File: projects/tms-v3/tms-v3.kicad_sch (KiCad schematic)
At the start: 55 parts, among them J1 ELEC_BATT, J10 XBee_R, J2 IGN_BATT, J3 LOAD_CELL, J4 PRESSURE, J5 ARM_SW, J6 IGNITER, J7 Teensy4.1_L, J8 Teensy4.1_R, J9 XBee_L, K1 HF46F, Q1 MMBT3904, U2A ADS1256_L, U2B ADS1256_R, U3 ADS1220IPWR, U4 LM7805, Y1 7.68MHz

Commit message: PCB workspace: scoped escape hatch, hardened gates, repo cleanup
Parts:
- removed D1: 1N4148WS, Diode_SMD:D_SOD-323, symbol Diode:1N4148WS
- removed J10: XBee_R, Connector_PinSocket_2.54mm:PinSocket_1x10_P2.54mm_Vertical, symbol Connector_Generic:Conn_01x10
- removed J9: XBee_L, Connector_PinSocket_2.54mm:PinSocket_1x10_P2.54mm_Vertical, symbol Connector_Generic:Conn_01x10
- removed K1: HF46F, symbol Connector_Generic:Conn_01x05
- removed Q1: MMBT3904, Package_TO_SOT_SMD:SOT-23, symbol Transistor_BJT:MMBT3904
- removed U2A: ADS1256_L, symbol Connector_Generic:Conn_01x14
- removed U2B: ADS1256_R, symbol Connector_Generic:Conn_01x14
- removed U3: ADS1220IPWR, Package_SO:TSSOP-16_4.4x5mm_P0.65mm, symbol Analog_ADC:ADS1220xPW
- removed U4: LM7805, Package_TO_SOT_SMD:TO-263-3_TabPin2, symbol Regulator_Linear:L7805
- removed Y1: 7.68MHz, Crystal:Crystal_HC49-U_Vertical, symbol Device:Crystal
- added C11: 100nF, Capacitor_SMD:C_0402_1005Metric, symbol Device:C
- added C14, C6: 100nF, Capacitor_SMD:C_0603_1608Metric, symbol Device:C
- added C17: 10uF, Capacitor_SMD:C_0805_2012Metric, symbol Device:C
- added D1: 1N4148WS, jlcpcb:SOD-323_L1.8-W1.3-LS2.5-RD-1, symbol jlcpcb:1N4148WS-C57759
- added D2: PESD5V0S2BT, jlcpcb:SOT-23_L2.9-W1.3-P1.90-LS2.4-BR, symbol jlcpcb:PESD5V0S2BT,215
- added D3: SS54, jlcpcb:SMA_L4.4-W2.8-LS5.4-R-RD, symbol jlcpcb:SS54_C22452
- added J9: XBEE3, tms:XBee_THT_20pin_P2.00mm, symbol Connector_Generic:Conn_02x10_Counter_Clockwise
- added K1: HF46F-G/5-HS1T, jlcpcb:RELAYS-TH_HF46F-G-XX-HS1-XXX, symbol jlcpcb:HF46F-G_5-HS1T_C5274026
- added L1: 10uH, Inductor_SMD:L_0805_2012Metric, symbol Device:L
- added Q1: MMBT3904, jlcpcb:SOT-23-3_L2.9-W1.3-P1.90-LS2.4-BR, symbol jlcpcb:MMBT3904-C20526
- added R10, R11, R12, R13, R14, R9: 33R, Resistor_SMD:R_0402_1005Metric, symbol Device:R
- added U2: ADS1256IDBR, jlcpcb:SSOP-28_L10.2-W5.3-P0.65-LS7.8-BL, symbol jlcpcb:ADS1256IDBR
- added U3: ADS1220IPWR, jlcpcb:TSSOP-16_L5.0-W4.4-P0.65-LS6.4-BL, symbol jlcpcb:ADS1220IPWR
- added U4: LM7805, jlcpcb:TO-263-2_L10.1-W9.1-P5.08-LS15.2-BR-1, symbol jlcpcb:LM7805_C22467097
- added Y1: 7.68MHz, jlcpcb:CRYSTAL-SMD_L11.4-W4.7-LS12.4, symbol jlcpcb:AT-41CD2-7.68MHZ
- C10: footprint Capacitor_SMD:C_0603_1608Metric -> Capacitor_SMD:C_0402_1005Metric
- C8, C9: value 22pF -> 33pF
- H1: value MH1 -> M3
- H2: value MH2 -> M3
- H3: value MH3 -> M3
- H4: value MH4 -> M3
- J1: value ELEC_BATT -> XT30PW-ELEC; footprint (none) -> Connector_AMASS:AMASS_XT30PW-F_1x02_P2.50mm_Horizontal
- J2: value IGN_BATT -> XT30PW-IGN; footprint (none) -> Connector_AMASS:AMASS_XT30PW-F_1x02_P2.50mm_Horizontal
- J3: value LOAD_CELL -> LOAD-CELL; footprint (none) -> Connector_JST:JST_XH_B5B-XH-A_1x05_P2.50mm_Vertical
- J4: footprint (none) -> Connector_JST:JST_XH_B3B-XH-A_1x03_P2.50mm_Vertical
- J5: value ARM_SW -> ARM-SW; footprint (none) -> TerminalBlock_Phoenix:TerminalBlock_Phoenix_MKDS-1,5-2-5.08_1x02_P5.08mm_Horizontal
- J6: value IGNITER -> IGN-OUT; footprint (none) -> Connector_AMASS:AMASS_XT60-F_1x02_P7.20mm_Vertical
- J7: value Teensy4.1_L -> TEENSY-L
- J8: value Teensy4.1_R -> TEENSY-R
- LED1: value PWR_GRN -> GREEN
- LED2: value ARM_RED -> RED
- LED3: value TX_YLW -> YELLOW
- TP1: value TP_VBAT -> VBAT
- TP2: value TP_5V -> +5V
- TP3: value TP_3V3 -> +3V3
- TP4: value TP_AINP -> AINP
- TP5: value TP_AINN -> AINN
- TP6: value TP_PRES -> PRES
- TP7: value TP_DRDY1 -> DRDY1
- TP8: value TP_DRDY2 -> DRDY2
- TP9: value TP_RELAY -> RELAY
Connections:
- net +3V3: now also C13.1, C5.1, J7.3 (Pin_3), J8.15 (Pin_15), TP3.1 (Pin_1), C11.1, C14.1, C6.1, J9.1 (Pin_1), U2.14 (SYNCPDWN), U2.15 (RESET), U2.16 (DVDD), U3.13 (DVDD)
- net +5V: now also C1.1, C10.1, C12.1, C16.1, C2.1, C3.1, C4.1, J7.1 (Pin_1), TP2.1 (Pin_1), D1.2 (A), K1.1, L1.1, U2.1 (AVDD), U3.12 (AVDD), U4.3 (OUT)
- net ADS1220_CS: now also J8.2 (Pin_2), U3.2 (~{CS})
- net ADS1220_DRDY: now also J8.8 (Pin_8), TP8.1 (Pin_1), U3.14 (~{DRDY})
- net ADS1256_CS: now also J8.12 (Pin_12), U2.20 (CS)
- net ADS1256_DRDY: now also J8.11 (Pin_11), TP7.1 (Pin_1), U2.21 (DRDY)
- net GND: now also C1.2, C10.2, C12.2, C13.2, C15.2, C16.2, C2.2, C3.2, C4.2, C5.2, C8.2, C9.2, J1.2 (Pin_2), J3.2 (Pin_2), J3.5 (Pin_5), J4.3 (Pin_3), J7.15 (Pin_15), J7.2 (Pin_2), J8.1 (Pin_1), LED1.1 (K), LED2.1 (K), LED3.1 (K), R2.2, C11.2, C14.2, C17.2, C6.2, D2.3, J9.10 (Pin_10), Q1.2 (E), U2.17 (DGND), U2.2 (AGND), U2.5 (AINCOM), U3.10 (AIN1), U3.3 (CLK), U3.4 (DGND), U3.5 (AVSS), U4.2 (GND)
- net IGN_OUT: now also J6.1 (Pin_1), K1.3
- net LC_AINN: now also R4.2, U2.7 (AIN1)
- net LC_AINP: now also R3.2, U2.6 (AIN0)
- net PRES_SIG: now also R5.2, U3.7 (AIN2)
- net RELAY_CTRL: now also J8.4 (Pin_4), R1.1, TP9.1 (Pin_1)
- net SPI0_MISO: now also J8.14 (Pin_14), R10.1
- net SPI0_MOSI: now also J8.13 (Pin_13), R9.2
- net SPI0_SCK: now also J7.14 (Pin_14), R11.2
- net SPI1_MISO: now also J8.3 (Pin_3), R13.1
- net SPI1_MOSI: now also J8.18 (Pin_18), R12.2
- net SPI1_SCK: now also J8.19 (Pin_19), R14.2
- net UART2_RX: now also J8.9 (Pin_9), J9.2 (Pin_2)
- net UART2_TX: now also J8.10 (Pin_10), J9.3 (Pin_3)
- net VBAT: now also J1.1 (Pin_1), J4.1 (Pin_1), TP1.1 (Pin_1), D3.1 (A)
- net IGN_BATT+: now reaches J2.1 (Pin_1)
- net IGN_BATT+: now also J5.1 (Pin_1)
- net IGN_GND: now reaches J2.2 (Pin_2)
- net IGN_GND: now also J6.2 (Pin_2)
- net LED_TX_A: now reaches LED3.2 (A)
- net LED_TX_A: now also R8.2
- net XTAL1: now reaches C8.1
- net XTAL1: now also U2.19 (XTAL1CLKIN), Y1.1
- net +5V_FILT: now reaches J3.1 (Pin_1)
- net +5V_FILT: now also C17.1, L1.2
- net LC_SIG_P: now reaches J3.3 (Pin_3)
- net LC_SIG_P: now also R3.1, TP4.1 (Pin_1), D2.1
- net LC_SIG_N: now reaches J3.4 (Pin_4)
- net LC_SIG_N: now also R4.1, TP5.1 (Pin_1), D2.2
- net LED_TX: now reaches R8.1
- net LED_TX: now also J8.7 (Pin_7)
- net NPN_BASE: now reaches R1.2
- net NPN_BASE: now also R2.1, Q1.1 (B)
- net LED_PWR: now reaches J8.5 (Pin_5)
- net LED_PWR: now also R6.1
- net LED_ARM: now reaches J8.6 (Pin_6)
- net LED_ARM: now also R7.1
- net IGN_ARM_RET: now reaches J5.2 (Pin_2)
- net IGN_ARM_RET: now also K1.2
- net LED_ARM_A: now reaches LED2.2 (A)
- net LED_ARM_A: now also R7.2
- net VBAT_PROT: now reaches C15.1
- net VBAT_PROT: now also D3.2 (K), U4.1 (IN)
- net PRES_RAW: now reaches R5.1
- net PRES_RAW: now also J4.2 (Pin_2), TP6.1 (Pin_1)
- net VREF_P: now reaches C7.1
- net VREF_P: now also U2.4 (VREFP)
- net VREF_N: now reaches C7.2
- net VREF_N: now also U2.3 (VREFN)
- net XTAL2: now reaches C9.1
- net XTAL2: now also U2.18 (XTAL2), Y1.2
- net LED_PWR_A: now reaches R6.2
- net LED_PWR_A: now also LED1.2 (A)
- new net ADS1220_DIN_ADC: R12.1, U3.16 (DIN)
- new net ADS1220_DOUT_ADC: R13.2, U3.15 (DOUT/~{DRDY})
- new net ADS1220_SCLK_ADC: R14.1, U3.1 (SCLK)
- new net ADS1256_DIN_ADC: R9.1, U2.23 (DIN)
- new net ADS1256_DOUT_ADC: R10.2, U2.22 (DOUT)
- new net ADS1256_SCLK_ADC: R11.1, U2.24 (SCLK)
- new net RELAY_COIL_SW: D1.1 (C), K1.6, Q1.3 (C)
- no-connect marks 0 -> 60

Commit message: 9/6 update
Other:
- company: (none) -> PSI Rocketry
- title: (none) -> TMS V3 - Thrust Measurement System

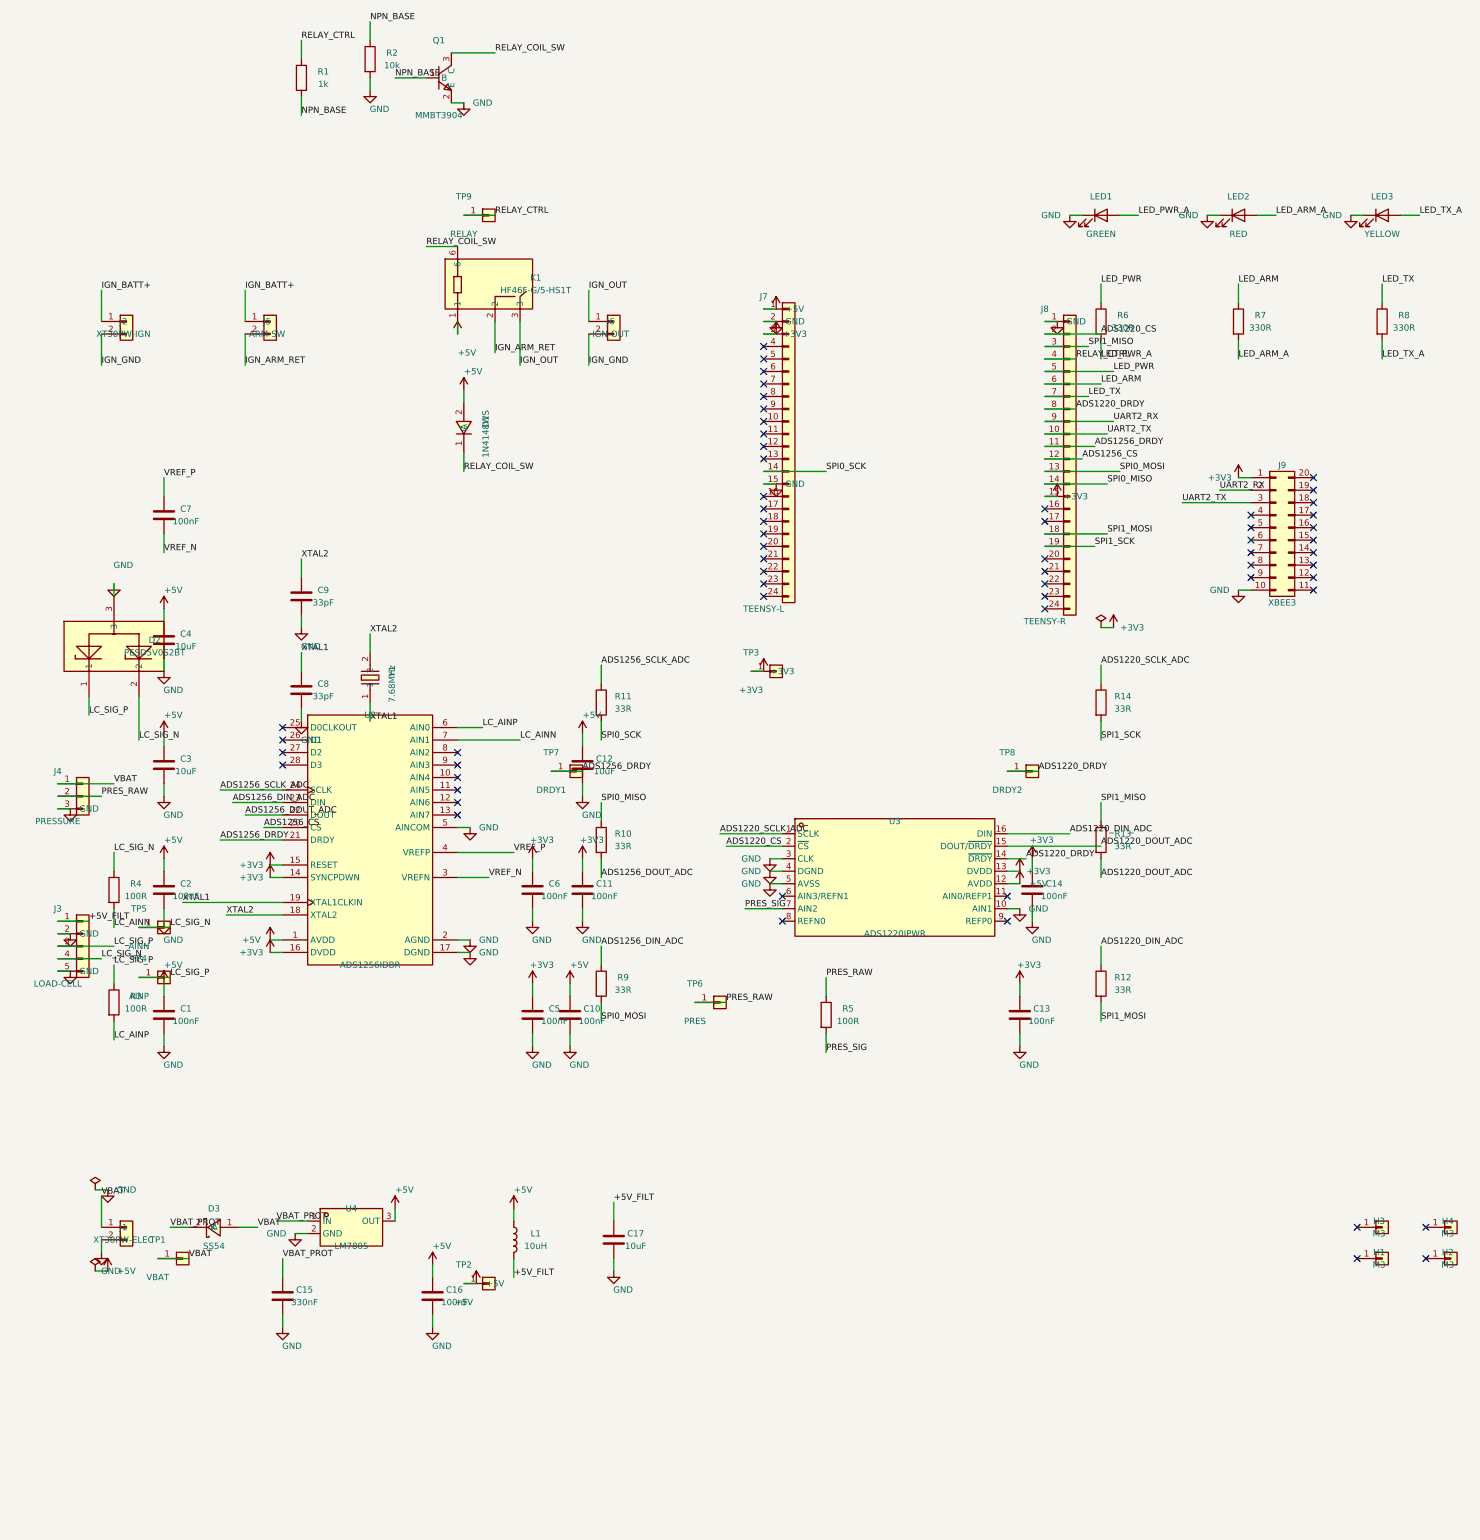
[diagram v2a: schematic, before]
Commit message: feat: promote TMS hierarchy with safe board net reconciliation
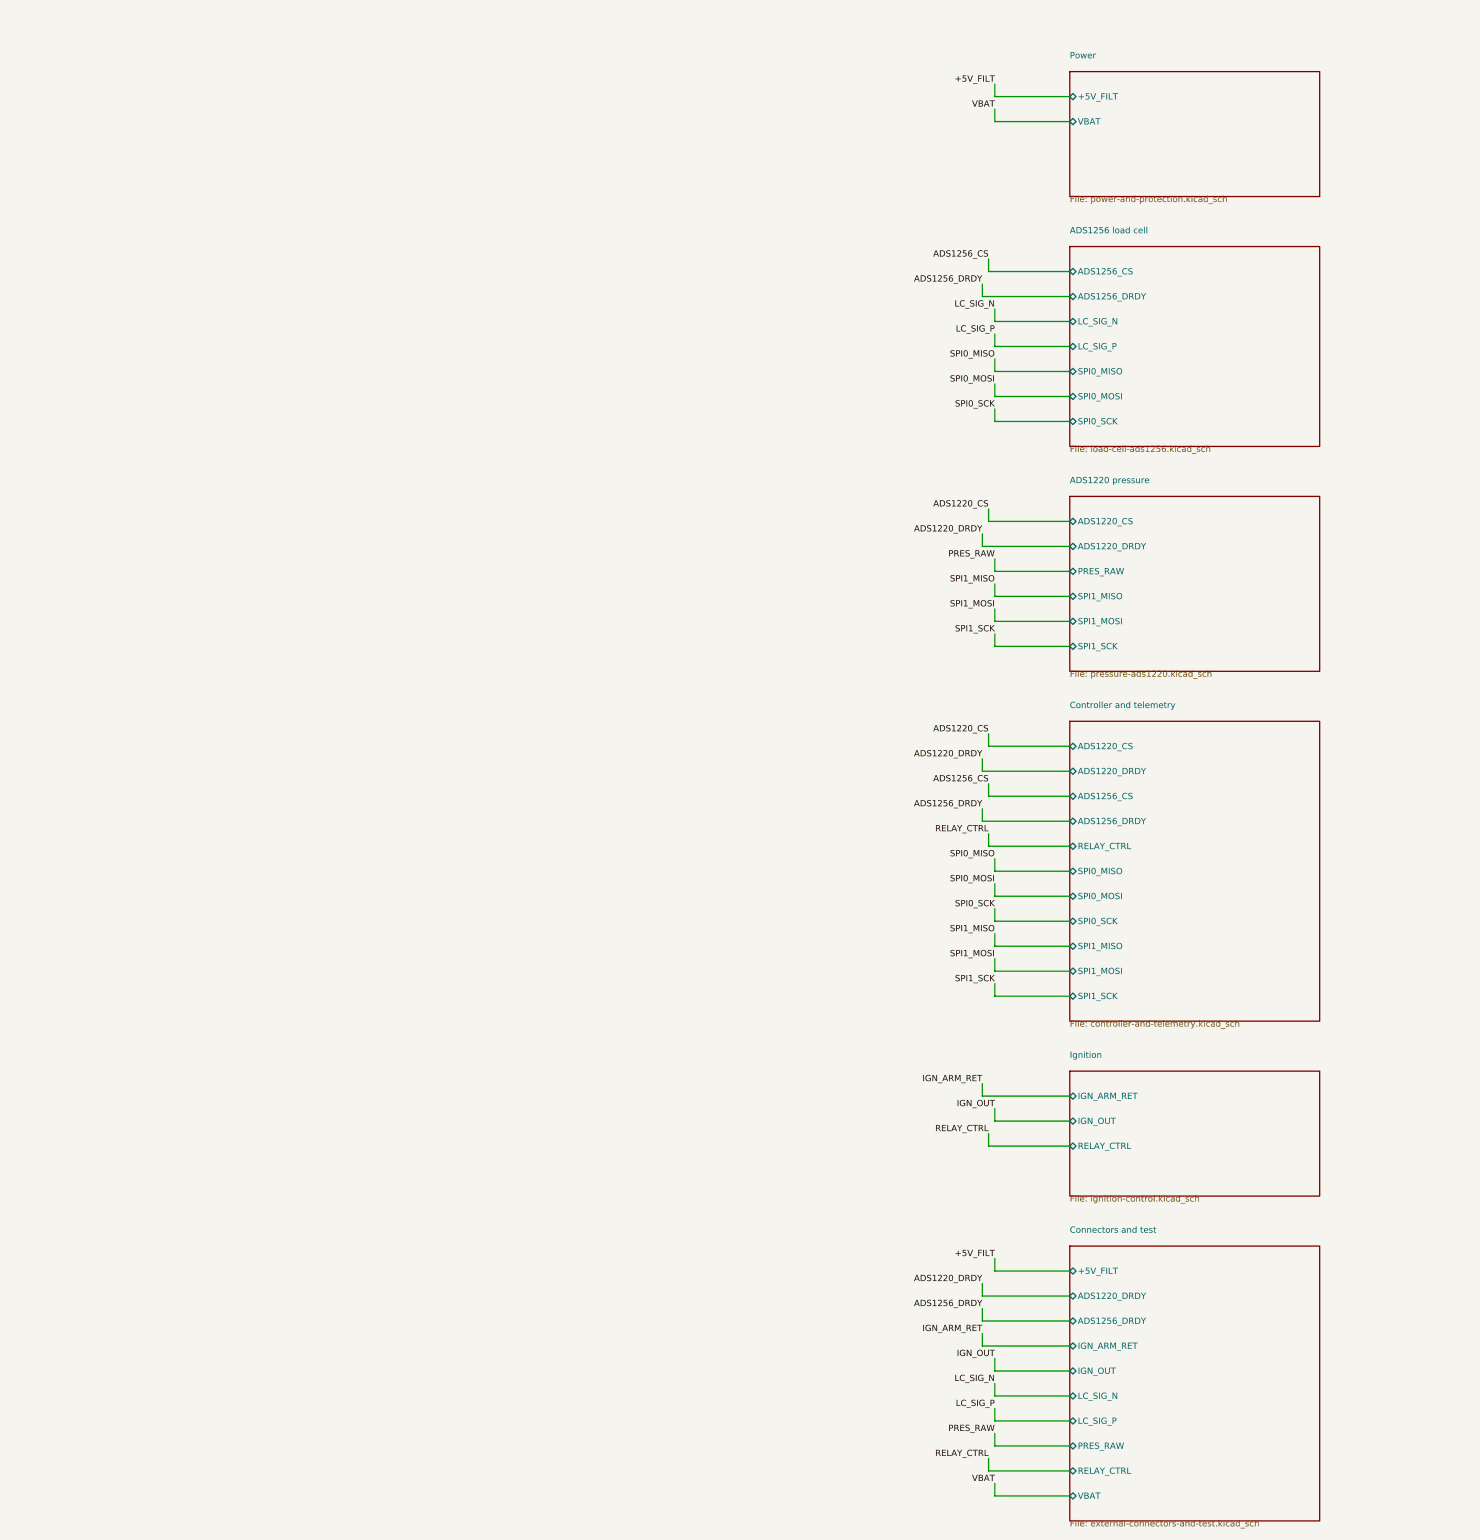
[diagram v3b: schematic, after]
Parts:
- removed C1, C13, C14, C16, C2, C5, C6, C7: 100nF, Capacitor_SMD:C_0603_1608Metric, symbol Device:C
- removed C10, C11: 100nF, Capacitor_SMD:C_0402_1005Metric, symbol Device:C
- removed C12, C17, C3, C4: 10uF, Capacitor_SMD:C_0805_2012Metric, symbol Device:C
- removed C15: 330nF, Capacitor_SMD:C_0603_1608Metric, symbol Device:C
- removed C8, C9: 33pF, Capacitor_SMD:C_0402_1005Metric, symbol Device:C
- removed D1: 1N4148WS, jlcpcb:SOD-323_L1.8-W1.3-LS2.5-RD-1, symbol jlcpcb:1N4148WS-C57759
- removed D2: PESD5V0S2BT, jlcpcb:SOT-23_L2.9-W1.3-P1.90-LS2.4-BR, symbol jlcpcb:PESD5V0S2BT,215
- removed D3: SS54, jlcpcb:SMA_L4.4-W2.8-LS5.4-R-RD, symbol jlcpcb:SS54_C22452
- removed H1, H2, H3, H4: M3, MountingHole:MountingHole_3.2mm_M3_Pad, symbol Connector_Generic:Conn_01x01
- removed J1: XT30PW-ELEC, Connector_AMASS:AMASS_XT30PW-F_1x02_P2.50mm_Horizontal, symbol Connector_Generic:Conn_01x02
- removed J2: XT30PW-IGN, Connector_AMASS:AMASS_XT30PW-F_1x02_P2.50mm_Horizontal, symbol Connector_Generic:Conn_01x02
- removed J3: LOAD-CELL, Connector_JST:JST_XH_B5B-XH-A_1x05_P2.50mm_Vertical, symbol Connector_Generic:Conn_01x05
- removed J4: PRESSURE, Connector_JST:JST_XH_B3B-XH-A_1x03_P2.50mm_Vertical, symbol Connector_Generic:Conn_01x03
- removed J5: ARM-SW, TerminalBlock_Phoenix:TerminalBlock_Phoenix_MKDS-1,5-2-5.08_1x02_P5.08mm_Horizontal, symbol Connector_Generic:Conn_01x02
- removed J6: IGN-OUT, Connector_AMASS:AMASS_XT60-F_1x02_P7.20mm_Vertical, symbol Connector_Generic:Conn_01x02
- removed J7: TEENSY-L, Connector_PinSocket_2.54mm:PinSocket_1x24_P2.54mm_Vertical, symbol Connector_Generic:Conn_01x24
- removed J8: TEENSY-R, Connector_PinSocket_2.54mm:PinSocket_1x24_P2.54mm_Vertical, symbol Connector_Generic:Conn_01x24
- removed J9: XBEE3, tms:XBee_THT_20pin_P2.00mm, symbol Connector_Generic:Conn_02x10_Counter_Clockwise
- removed K1: HF46F-G/5-HS1T, jlcpcb:RELAYS-TH_HF46F-G-XX-HS1-XXX, symbol jlcpcb:HF46F-G_5-HS1T_C5274026
- removed L1: 10uH, Inductor_SMD:L_0805_2012Metric, symbol Device:L
- removed LED1: GREEN, LED_SMD:LED_0603_1608Metric, symbol Device:LED
- removed LED2: RED, LED_SMD:LED_0603_1608Metric, symbol Device:LED
- removed LED3: YELLOW, LED_SMD:LED_0603_1608Metric, symbol Device:LED
- removed Q1: MMBT3904, jlcpcb:SOT-23-3_L2.9-W1.3-P1.90-LS2.4-BR, symbol jlcpcb:MMBT3904-C20526
- removed R1: 1k, Resistor_SMD:R_0402_1005Metric, symbol Device:R
- removed R10, R11, R12, R13, R14, R9: 33R, Resistor_SMD:R_0402_1005Metric, symbol Device:R
- removed R2: 10k, Resistor_SMD:R_0402_1005Metric, symbol Device:R
- removed R3, R4, R5: 100R, Resistor_SMD:R_0402_1005Metric, symbol Device:R
- removed R6, R7, R8: 330R, Resistor_SMD:R_0402_1005Metric, symbol Device:R
- removed TP1: VBAT, TestPoint:TestPoint_Pad_1.0x1.0mm, symbol Connector_Generic:Conn_01x01
- removed TP2: +5V, TestPoint:TestPoint_Pad_1.0x1.0mm, symbol Connector_Generic:Conn_01x01
- removed TP3: +3V3, TestPoint:TestPoint_Pad_1.0x1.0mm, symbol Connector_Generic:Conn_01x01
- removed TP4: AINP, TestPoint:TestPoint_Pad_1.0x1.0mm, symbol Connector_Generic:Conn_01x01
- removed TP5: AINN, TestPoint:TestPoint_Pad_1.0x1.0mm, symbol Connector_Generic:Conn_01x01
- removed TP6: PRES, TestPoint:TestPoint_Pad_1.0x1.0mm, symbol Connector_Generic:Conn_01x01
- removed TP7: DRDY1, TestPoint:TestPoint_Pad_1.0x1.0mm, symbol Connector_Generic:Conn_01x01
- removed TP8: DRDY2, TestPoint:TestPoint_Pad_1.0x1.0mm, symbol Connector_Generic:Conn_01x01
- removed TP9: RELAY, TestPoint:TestPoint_Pad_1.0x1.0mm, symbol Connector_Generic:Conn_01x01
- removed U2: ADS1256IDBR, jlcpcb:SSOP-28_L10.2-W5.3-P0.65-LS7.8-BL, symbol jlcpcb:ADS1256IDBR
- removed U3: ADS1220IPWR, jlcpcb:TSSOP-16_L5.0-W4.4-P0.65-LS6.4-BL, symbol jlcpcb:ADS1220IPWR
- removed U4: LM7805, jlcpcb:TO-263-2_L10.1-W9.1-P5.08-LS15.2-BR-1, symbol jlcpcb:LM7805_C22467097
- removed Y1: 7.68MHz, jlcpcb:CRYSTAL-SMD_L11.4-W4.7-LS12.4, symbol jlcpcb:AT-41CD2-7.68MHZ
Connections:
- no-connect marks 60 -> 0
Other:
- added sheet ADS1220 pressure (pressure-ads1220.kicad_sch)
- added sheet ADS1256 load cell (load-cell-ads1256.kicad_sch)
- added sheet Connectors and test (external-connectors-and-test.kicad_sch)
- added sheet Controller and telemetry (controller-and-telemetry.kicad_sch)
- added sheet Ignition (ignition-control.kicad_sch)
- added sheet Power (power-and-protection.kicad_sch)
- company: PSI Rocketry -> (none)
- title: TMS V3 - Thrust Measurement System -> TMS V3
